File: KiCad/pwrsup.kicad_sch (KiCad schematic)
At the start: 17 parts, among them U1 TLE2426xP, U2 L7805, U3 TLE2426xP, U4 TLE2426xP

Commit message: Made the board :D
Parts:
- U2: footprint Package_TO_SOT_THT:TO-218-3_Vertical -> Package_TO_SOT_THT:TO-218-3_Horizontal_TabDown
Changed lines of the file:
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@@
 			)
 		)
-		(property "Footprint" "Package_TO_SOT_THT:TO-218-3_Vertical"
+		(property "Footprint" "Package_TO_SOT_THT:TO-218-3_Horizontal_TabDown"
 			(at 69.215 25.4 0)
 			(effects

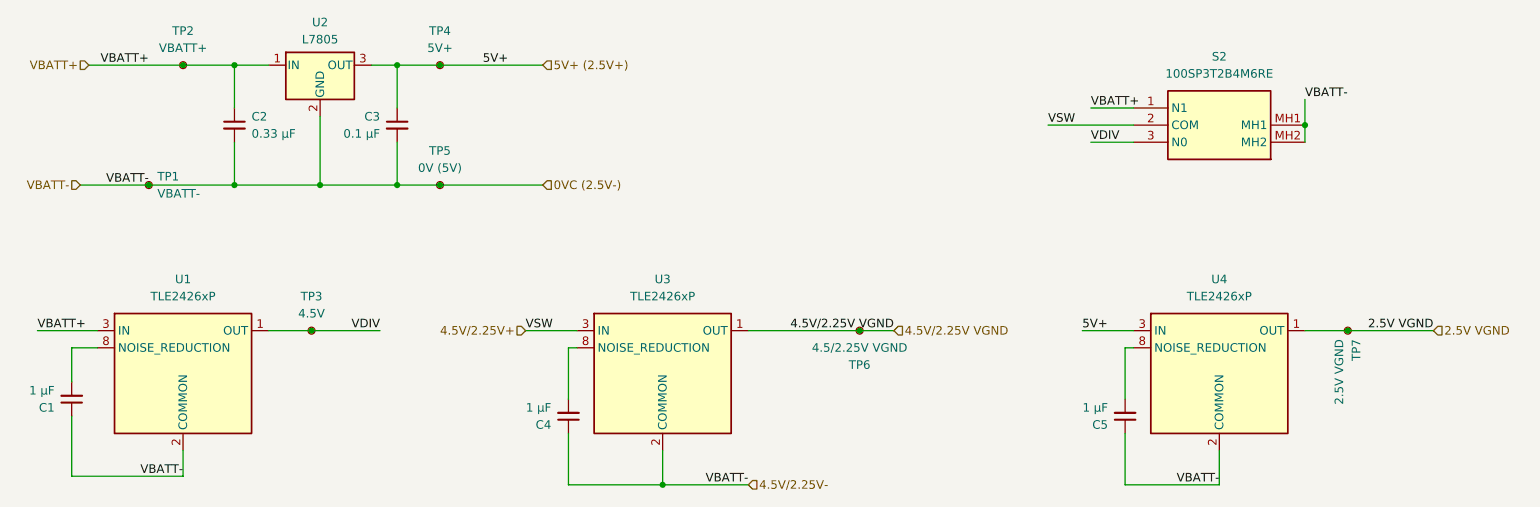
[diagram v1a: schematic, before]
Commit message: Added milling machine files / updated schematic+pcb annotations /  updated footprints
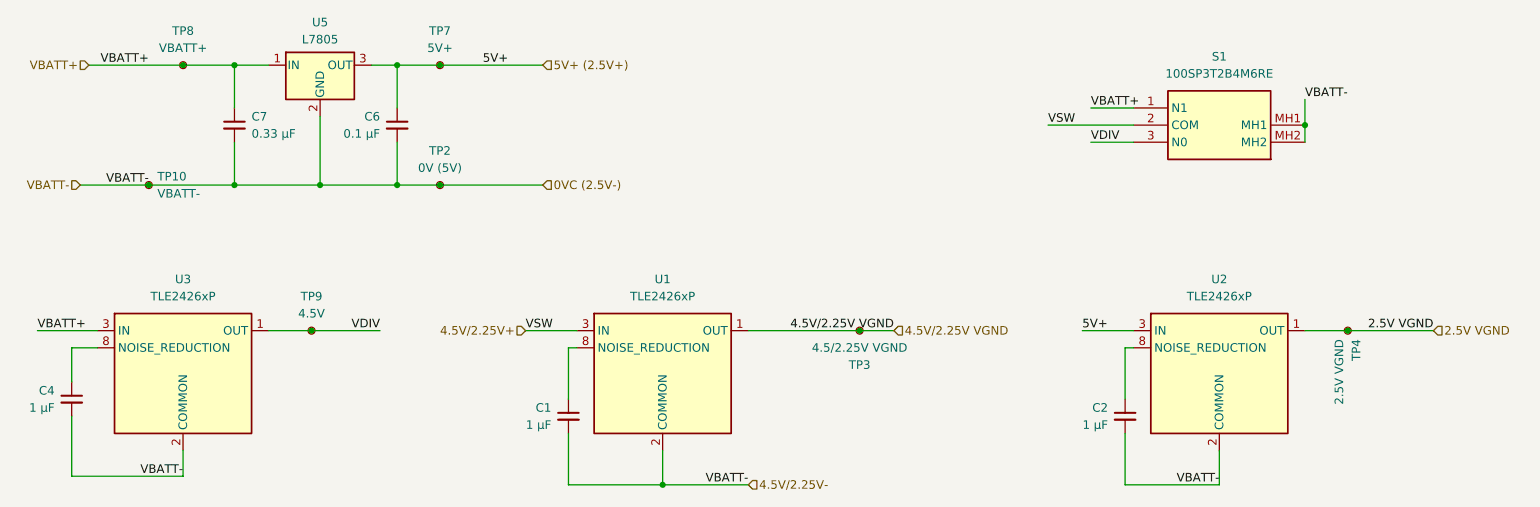
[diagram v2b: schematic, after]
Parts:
- U5: renamed from U2; footprint Package_TO_SOT_THT:TO-218-3_Horizontal_TabDown -> Package_TO_SOT_THT:TO-220-3_Horizontal_TabDown
- renumbered C4 to C1, C5 to C2, C1 to C4, C3 to C6, C2 to C7, S2 to S1, TP1 to TP10, TP5 to TP2, TP6 to TP3, TP7 to TP4, TP4 to TP7, TP2 to TP8, TP3 to TP9, U3 to U1, U4 to U2, U1 to U3
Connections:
- net 0VC (2.5V-): now also C1.2, C2.2, C4.2; no longer C1.1, C2.1, C4.1
- net at U1.8 (NOISE_REDUCTION): now also C1.1; no longer C1.2
- net at U2.8 (NOISE_REDUCTION): now also C2.1; no longer C2.2
- net at U3.8 (NOISE_REDUCTION): now also C4.1; no longer C4.2
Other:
- moved on the sheet: C1, C2, C4
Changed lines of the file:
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@@
 		(on_board yes)
 		(dnp no)
-		(property "Reference" "TP6"
+		(property "Reference" "TP3"
 			(at 148.59 66.04 90)
 			(effects
@@
 			(project "ChipTester_354"
 				(path "/57b9e980-cd8f-44e4-af61-2cbd5bb30325/462ebe9c-fcaa-4c45-9d51-a2484be3186e"
-					(reference "TP6")
+					(reference "TP3")
 					(unit 1)
 				)
@@
 	(symbol
 		(lib_id "Device:C_Small")
-		(at 105.41 73.66 180)
-		(unit 1)
-		(exclude_from_sim no)
-		(in_bom yes)
-		(on_board yes)
-		(dnp no)
-		(property "Reference" "C4"
-			(at 102.87 74.9238 0)
+		(at 105.41 73.66 0)
+		(mirror y)
+		(unit 1)
+		(exclude_from_sim no)
+		(in_bom yes)
+		(on_board yes)
+		(dnp no)
+		(property "Reference" "C1"
+			(at 102.87 72.3962 0)
 			(effects
 				(font
@@
 		)
 		(property "Value" "1 µF"
-			(at 102.87 72.3838 0)
+			(at 102.87 74.9362 0)
 			(effects
 				(font
@@
 			(project "ChipTester_354"
 				(path "/57b9e980-cd8f-44e4-af61-2cbd5bb30325/462ebe9c-fcaa-4c45-9d51-a2484be3186e"
-					(reference "C4")
+					(reference "C1")
 					(unit 1)
 				)
@@
 		(dnp no)
 		(fields_autoplaced yes)
-		(property "Reference" "TP3"
+		(property "Reference" "TP9"
 			(at 67.31 55.88 90)
 			(effects
@@
 			(project "ChipTester_354"
 				(path "/57b9e980-cd8f-44e4-af61-2cbd5bb30325/462ebe9c-fcaa-4c45-9d51-a2484be3186e"
-					(reference "TP3")
+					(reference "TP9")
 					(unit 1)
 				)
@@
 		(dnp no)
 		(fields_autoplaced yes)
-		(property "Reference" "U3"
+		(property "Reference" "U1"
 			(at 119.38 53.34 0)
 			(effects
@@
 			(project ""
 				(path "/57b9e980-cd8f-44e4-af61-2cbd5bb30325/462ebe9c-fcaa-4c45-9d51-a2484be3186e"
-					(reference "U3")
+					(reference "U1")
 					(unit 1)
 				)
@@
 		(dnp no)
 		(fields_autoplaced yes)
-		(property "Reference" "TP1"
+		(property "Reference" "TP10"
 			(at 44.45 38.0999 0)
 			(effects
@@
 			(project ""
 				(path "/57b9e980-cd8f-44e4-af61-2cbd5bb30325/462ebe9c-fcaa-4c45-9d51-a2484be3186e"
-					(reference "TP1")
+					(reference "TP10")
 					(unit 1)
 				)
@@
 		(dnp no)
 		(fields_autoplaced yes)
-		(property "Reference" "U2"
+		(property "Reference" "U5"
 			(at 68.58 15.24 0)
 			(effects
@@
 			)
 		)
-		(property "Footprint" "Package_TO_SOT_THT:TO-218-3_Horizontal_TabDown"
+		(property "Footprint" "Package_TO_SOT_THT:TO-220-3_Horizontal_TabDown"
 			(at 69.215 25.4 0)
 			(effects
@@
 			)
 		)
-		(property "Datasheet" "http://www.st.com/content/ccc/resource/technical/document/datasheet/41/4f/b3/b0/12/d4/47/88/CD00000444.pdf/files/CD00000444.pdf/jcr:content/translations/en.CD00000444.pdf"
+		(property "Datasheet" ""
 			(at 68.58 22.86 0)
 			(effects
@@
 			)
 		)
-		(property "Description" "Positive 1.5A 35V Linear Regulator, Fixed Output 5V, TO-220/TO-263/TO-252"
+		(property "Description" ""
 			(at 68.58 21.59 0)
 			(effects
@@
 			(project ""
 				(path "/57b9e980-cd8f-44e4-af61-2cbd5bb30325/462ebe9c-fcaa-4c45-9d51-a2484be3186e"
-					(reference "U2")
+					(reference "U5")
 					(unit 1)
 				)
@@
 		(dnp no)
 		(fields_autoplaced yes)
-		(property "Reference" "S2"
+		(property "Reference" "S1"
 			(at 201.93 20.32 0)
 			(effects
@@
 			(project "ChipTester_354"
 				(path "/57b9e980-cd8f-44e4-af61-2cbd5bb30325/462ebe9c-fcaa-4c45-9d51-a2484be3186e"
-					(reference "S2")
+					(reference "S1")
 					(unit 1)
 				)
@@
 		(on_board yes)
 		(dnp no)
-		(property "Reference" "C3"
+		(property "Reference" "C6"
 			(at 77.47 29.2162 0)
 			(effects
@@
 			(project "ChipTester_354"
 				(path "/57b9e980-cd8f-44e4-af61-2cbd5bb30325/462ebe9c-fcaa-4c45-9d51-a2484be3186e"
-					(reference "C3")
+					(reference "C6")
 					(unit 1)
 				)
@@
 		(dnp no)
 		(fields_autoplaced yes)
-		(property "Reference" "TP4"
+		(property "Reference" "TP7"
 			(at 86.36 16.51 90)
 			(effects
@@
 			(project ""
 				(path "/57b9e980-cd8f-44e4-af61-2cbd5bb30325/462ebe9c-fcaa-4c45-9d51-a2484be3186e"
-					(reference "TP4")
+					(reference "TP7")
 					(unit 1)
 				)
@@
 	(symbol
 		(lib_id "Device:C_Small")
-		(at 187.96 73.66 180)
-		(unit 1)
-		(exclude_from_sim no)
-		(in_bom yes)
-		(on_board yes)
-		(dnp no)
-		(property "Reference" "C5"
-			(at 185.42 74.9238 0)
+		(at 187.96 73.66 0)
+		(mirror y)
+		(unit 1)
+		(exclude_from_sim no)
+		(in_bom yes)
+		(on_board yes)
+		(dnp no)
+		(property "Reference" "C2"
+			(at 185.42 72.3962 0)
 			(effects
 				(font
@@
 		)
 		(property "Value" "1 µF"
-			(at 185.42 72.3838 0)
+			(at 185.42 74.9362 0)
 			(effects
 				(font
@@
 			(project "ChipTester_354"
 				(path "/57b9e980-cd8f-44e4-af61-2cbd5bb30325/462ebe9c-fcaa-4c45-9d51-a2484be3186e"
-					(reference "C5")
+					(reference "C2")
 					(unit 1)
 				)
@@
 		(on_board yes)
 		(dnp no)
-		(property "Reference" "TP7"
+		(property "Reference" "TP4"
 			(at 222.2501 62.23 90)
 			(effects
@@
 			(project "ChipTester_354"
 				(path "/57b9e980-cd8f-44e4-af61-2cbd5bb30325/462ebe9c-fcaa-4c45-9d51-a2484be3186e"
-					(reference "TP7")
+					(reference "TP4")
 					(unit 1)
 				)
@@
 	(symbol
 		(lib_id "Device:C_Small")
-		(at 31.75 71.12 180)
-		(unit 1)
-		(exclude_from_sim no)
-		(in_bom yes)
-		(on_board yes)
-		(dnp no)
-		(property "Reference" "C1"
-			(at 29.21 72.3838 0)
+		(at 31.75 71.12 0)
+		(mirror y)
+		(unit 1)
+		(exclude_from_sim no)
+		(in_bom yes)
+		(on_board yes)
+		(dnp no)
+		(property "Reference" "C4"
+			(at 29.21 69.8562 0)
 			(effects
 				(font
@@
 		)
 		(property "Value" "1 µF"
-			(at 29.21 69.8438 0)
+			(at 29.21 72.3962 0)
 			(effects
 				(font
@@
 			(project "ChipTester_354"
 				(path "/57b9e980-cd8f-44e4-af61-2cbd5bb30325/462ebe9c-fcaa-4c45-9d51-a2484be3186e"
-					(reference "C1")
+					(reference "C4")
 					(unit 1)
 				)
@@
 		(on_board yes)
 		(dnp no)
-		(fields_autoplaced yes)
-		(property "Reference" "C2"
+		(property "Reference" "C7"
 			(at 58.42 29.2162 0)
 			(effects
@@
 			(project ""
 				(path "/57b9e980-cd8f-44e4-af61-2cbd5bb30325/462ebe9c-fcaa-4c45-9d51-a2484be3186e"
-					(reference "C2")
+					(reference "C7")
 					(unit 1)
 				)
@@
 		(dnp no)
 		(fields_autoplaced yes)
-		(property "Reference" "U1"
+		(property "Reference" "U3"
 			(at 48.26 53.34 0)
 			(effects
@@
 			(project "ChipTester_354"
 				(path "/57b9e980-cd8f-44e4-af61-2cbd5bb30325/462ebe9c-fcaa-4c45-9d51-a2484be3186e"
-					(reference "U1")
+					(reference "U3")
 					(unit 1)
 				)
@@
 		(dnp no)
 		(fields_autoplaced yes)
-		(property "Reference" "TP5"
+		(property "Reference" "TP2"
 			(at 86.36 34.29 90)
 			(effects
@@
 			(project "ChipTester_354"
 				(path "/57b9e980-cd8f-44e4-af61-2cbd5bb30325/462ebe9c-fcaa-4c45-9d51-a2484be3186e"
-					(reference "TP5")
+					(reference "TP2")
 					(unit 1)
 				)
@@
 		(dnp no)
 		(fields_autoplaced yes)
-		(property "Reference" "TP2"
+		(property "Reference" "TP8"
 			(at 48.26 16.51 90)
 			(effects
@@
 			(project ""
 				(path "/57b9e980-cd8f-44e4-af61-2cbd5bb30325/462ebe9c-fcaa-4c45-9d51-a2484be3186e"
-					(reference "TP2")
+					(reference "TP8")
 					(unit 1)
 				)
@@
 		(dnp no)
 		(fields_autoplaced yes)
-		(property "Reference" "U4"
+		(property "Reference" "U2"
 			(at 201.93 53.34 0)
 			(effects
@@
 			(project "ChipTester_354"
 				(path "/57b9e980-cd8f-44e4-af61-2cbd5bb30325/462ebe9c-fcaa-4c45-9d51-a2484be3186e"
-					(reference "U4")
-					(unit 1)
-				)
+					(reference "U2")
+					(unit 1)
+				)
